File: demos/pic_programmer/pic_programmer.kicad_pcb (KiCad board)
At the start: 2 copper layers, 160 x 99.1 mm, 63 parts, among them J1 DB9-FEMAL, P1 CONN_2, P101 CONN_1, P102 CONN_1, P103 CONN_1, P104 CONN_1, P105 CONN_1, P106 CONN_1, P2 SUPP28, P3 SUPP40, Q1 BC237, Q2 BC307, Q3 BC307, U1 24Cxx, U2 74HC125, U3 7805, U4 LT1373, U5 PIC_18_PINS, U6 PIC_8_PINS

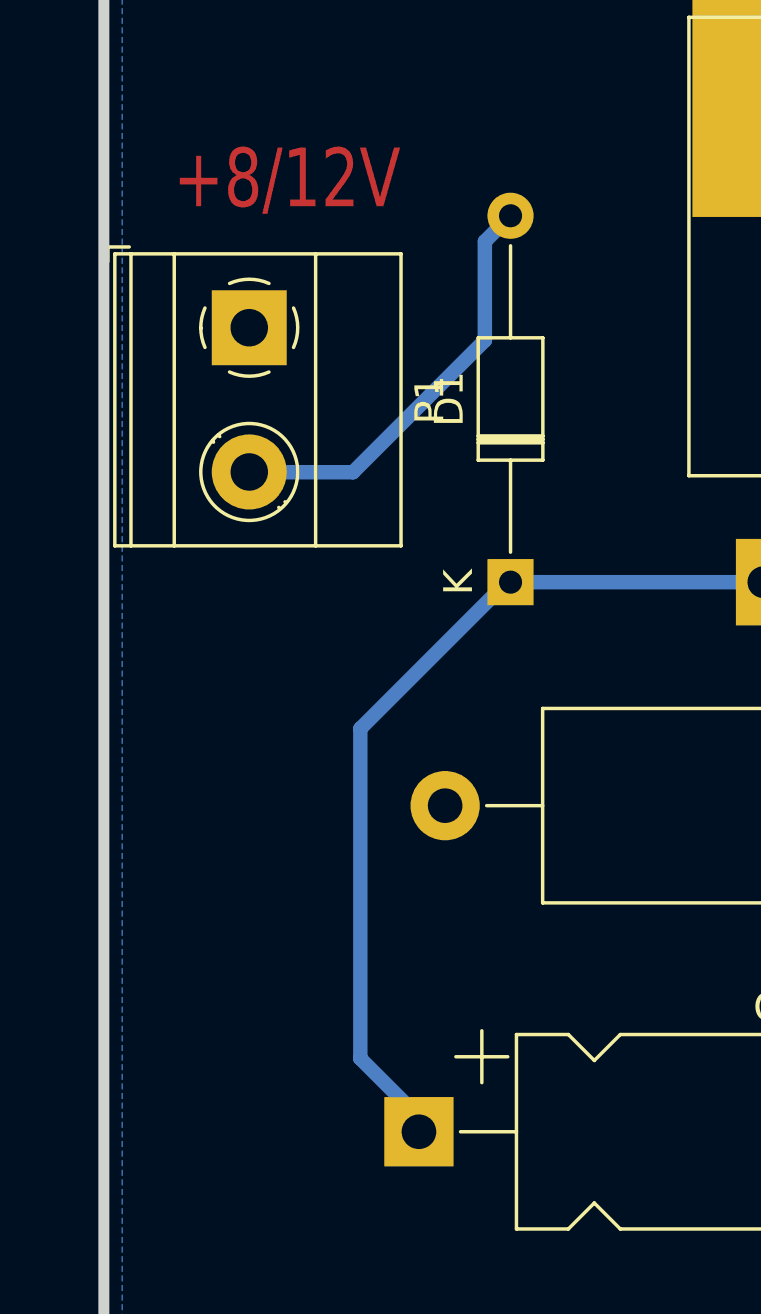
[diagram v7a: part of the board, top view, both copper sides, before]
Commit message: Update demos to use recent footprints.
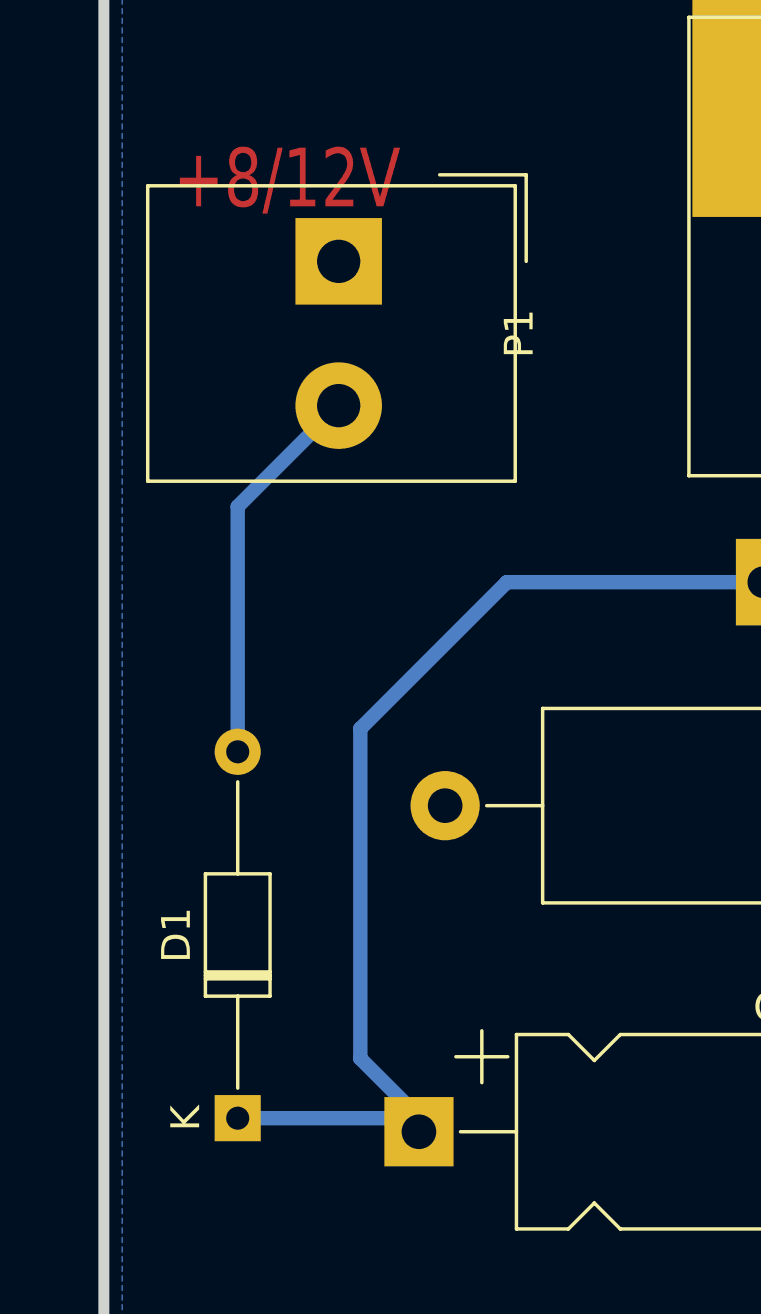
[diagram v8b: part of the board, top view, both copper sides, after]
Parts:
- P1: footprint TerminalBlock_Phoenix:TerminalBlock_Phoenix_MKDS-1,5-2_1x02_P5.00mm_Horizontal -> TerminalBlock_Altech:Altech_AK300_1x02_P5.00mm_45-Degree
- moved D1 20.8 mm to (78.3, 89.7)
- moved P1 3.86 mm to (81.8, 60.0)
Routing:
- net Net-(C2-Pad1): track 30.8 -> 37.3 mm
- net Net-(D1-Pad2): track 14.7 -> 13.4 mm
